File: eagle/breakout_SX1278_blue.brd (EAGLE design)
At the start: 28.6 x 28.6 mm, 19 parts, among them X1 734120110

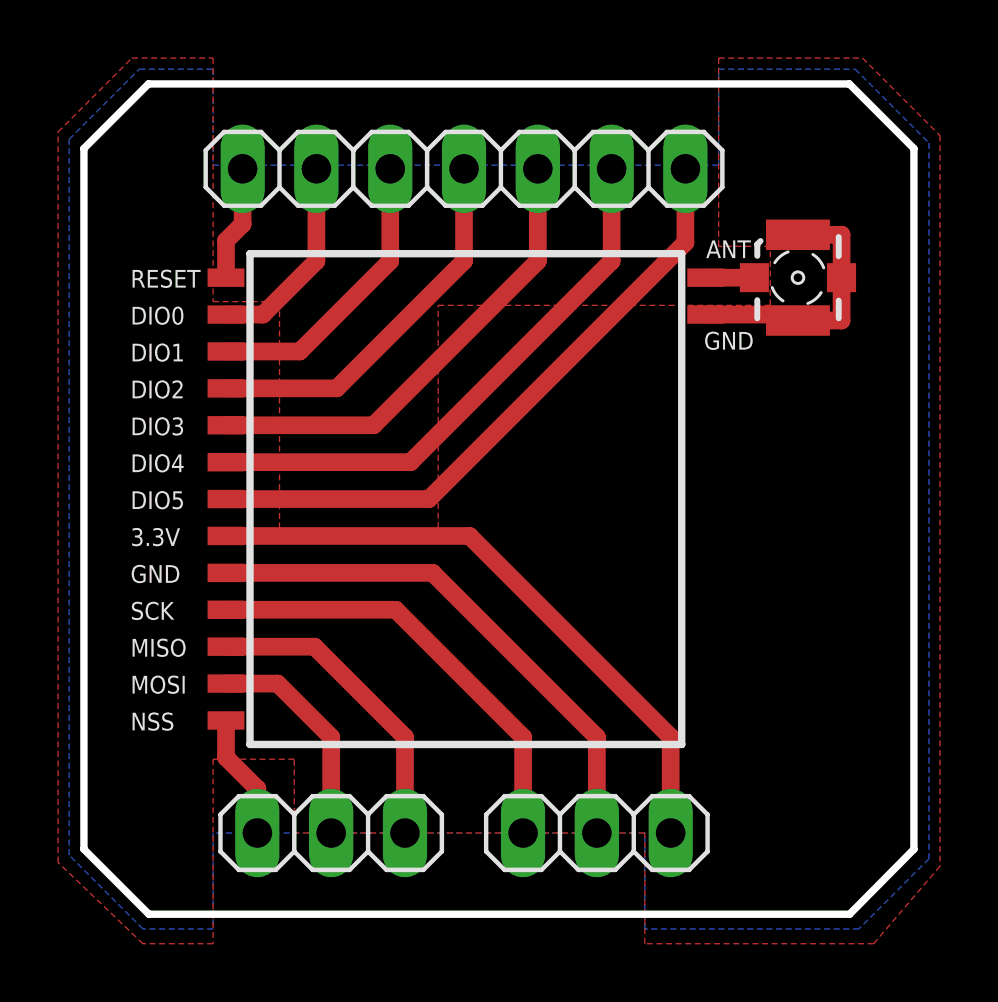
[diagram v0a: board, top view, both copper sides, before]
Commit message: Added SX1278 outline as an orientation marker
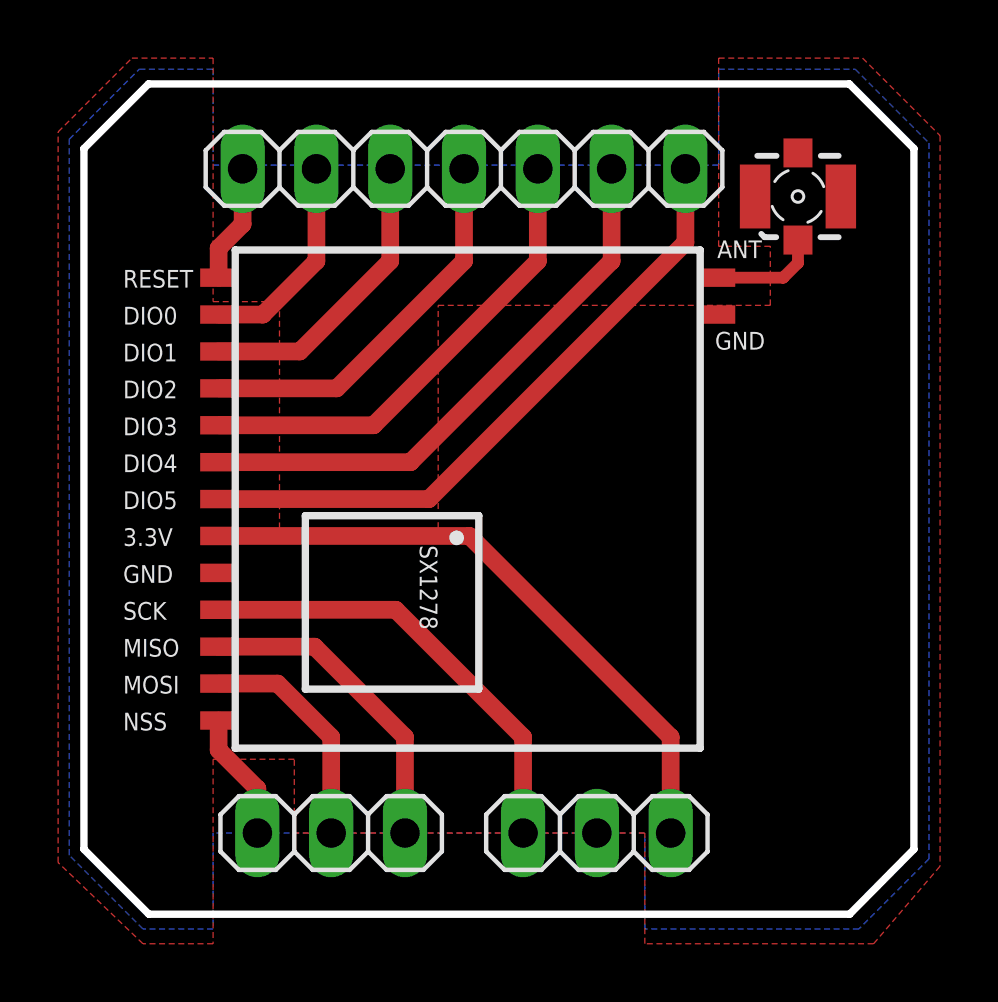
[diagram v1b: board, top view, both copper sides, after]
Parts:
- moved X1 2.79 mm to (24.6, 24.7), turned to 0 degrees
- moved ANT 0.38 mm to (21.8, 21.9)
- moved GND_A 0.38 mm to (21.8, 20.6)
- moved 3.3V 0.25 mm to (4.64, 13.0)
- moved DIO0 0.25 mm to (4.64, 20.6)
- moved DIO1 0.25 mm to (4.64, 19.4)
- moved DIO2 0.25 mm to (4.64, 18.1)
- moved DIO3 0.25 mm to (4.64, 16.8)
- moved DIO4 0.25 mm to (4.64, 15.6)
- moved DIO5 0.25 mm to (4.64, 14.3)
- moved GND 0.25 mm to (4.64, 11.7)
- moved MISO 0.25 mm to (4.64, 9.21)
- moved MOSI 0.25 mm to (4.64, 7.94)
- moved NSS 0.25 mm to (4.64, 6.67)
- moved RESET 0.25 mm to (4.64, 21.9)
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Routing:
- net GND: track 27.6 -> 0.00 mm
- net ANT: track 1.68 -> 3.79 mm
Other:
- board text added: "SX1278"

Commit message: Module layout update
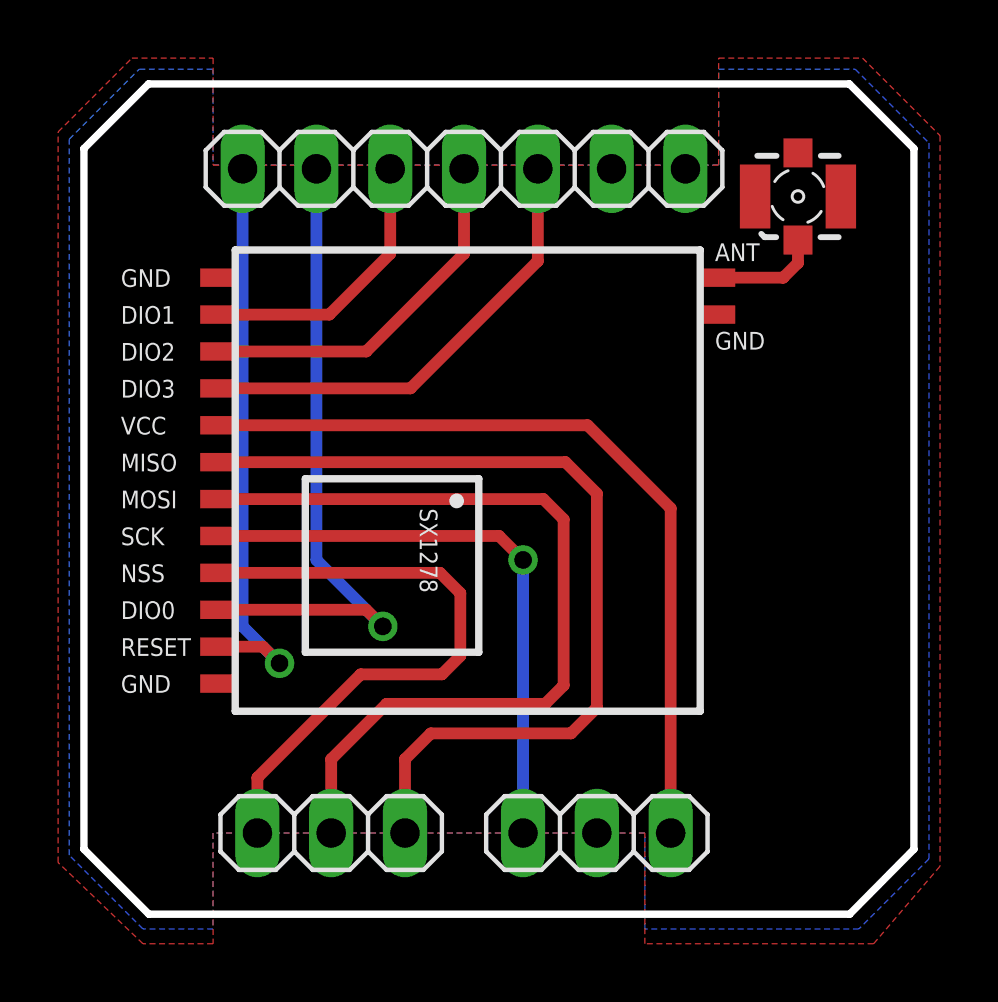
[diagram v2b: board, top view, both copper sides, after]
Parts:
- removed 3.3V, DIO4, DIO5: (no value), wirepad:SMD0,65-1,27
- added GND2, VCC: (no value), wirepad:SMD0,65-1,27
- moved RESET 12.7 mm to (4.64, 9.21)
- moved DIO0 10.2 mm to (4.64, 10.5)
- moved GND 10.2 mm to (4.64, 21.9)
- moved MISO 6.35 mm to (4.64, 15.6)
- moved MOSI 6.35 mm to (4.64, 14.3)
- moved NSS 5.08 mm to (4.64, 11.7)
- moved SCK 2.54 mm to (4.64, 13.0)
- moved DIO1 1.27 mm to (4.64, 20.6)
- moved DIO2 1.27 mm to (4.64, 19.4)
- moved DIO3 1.27 mm to (4.64, 18.1)
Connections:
- removed net DIO4: DIO4.1, JP1.6
- removed net DIO5: DIO5.1, JP1.7
- net 3.3V: now also VCC.1; no longer 3.3V.1
- net GND: now also GND2.1
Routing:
- net DIO5: track 22.3 -> 0.00 mm
- net MOSI: track 7.94 -> 29.5 mm
- net MISO: track 11.0 -> 30.7 mm
- net DIO4: track 19.6 -> 0.00 mm
- net NSS: track 4.43 -> 21.4 mm
- net RESET: track 4.09 -> 19.9 mm, vias 0 -> 1
- net DIO0: track 7.30 -> 22.6 mm, vias 0 -> 1
- net 3.3V: track 21.7 -> 27.9 mm
- net SCK: track 15.6 -> 20.2 mm, vias 0 -> 1
- net DIO2: track 13.4 -> 12.8 mm
- net DIO1: track 10.4 -> 9.69 mm
- net DIO3: track 16.5 -> 16.0 mm
